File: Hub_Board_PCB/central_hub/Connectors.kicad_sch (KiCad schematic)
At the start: 16 parts, among them J1 CX90B-16P, J10 Conn_02x03_Counter_Clockwise, J3 TSM-105-01-S-DV-M-TR, J4 Screw_Terminal_01x08, J5 PH2-06-UA, J6 Screw_Terminal_01x04, J7 Screw_Terminal_01x14, SW1 RotaryEncoder_Switch

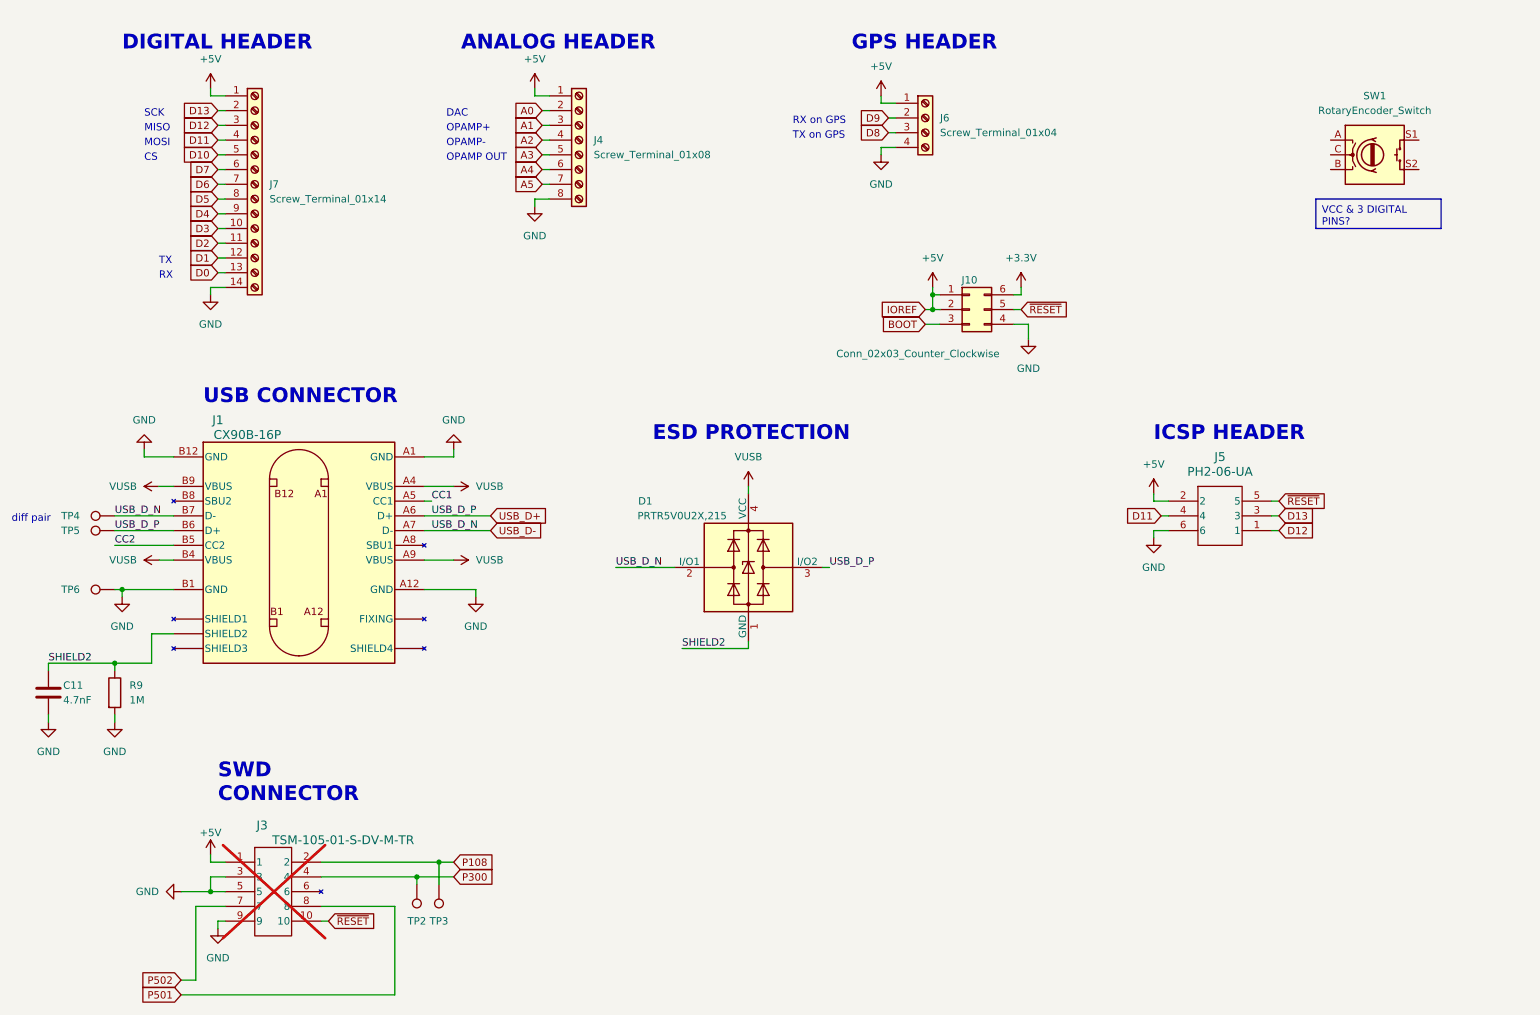
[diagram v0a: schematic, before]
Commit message: - added header for shorting VUSB and +5V
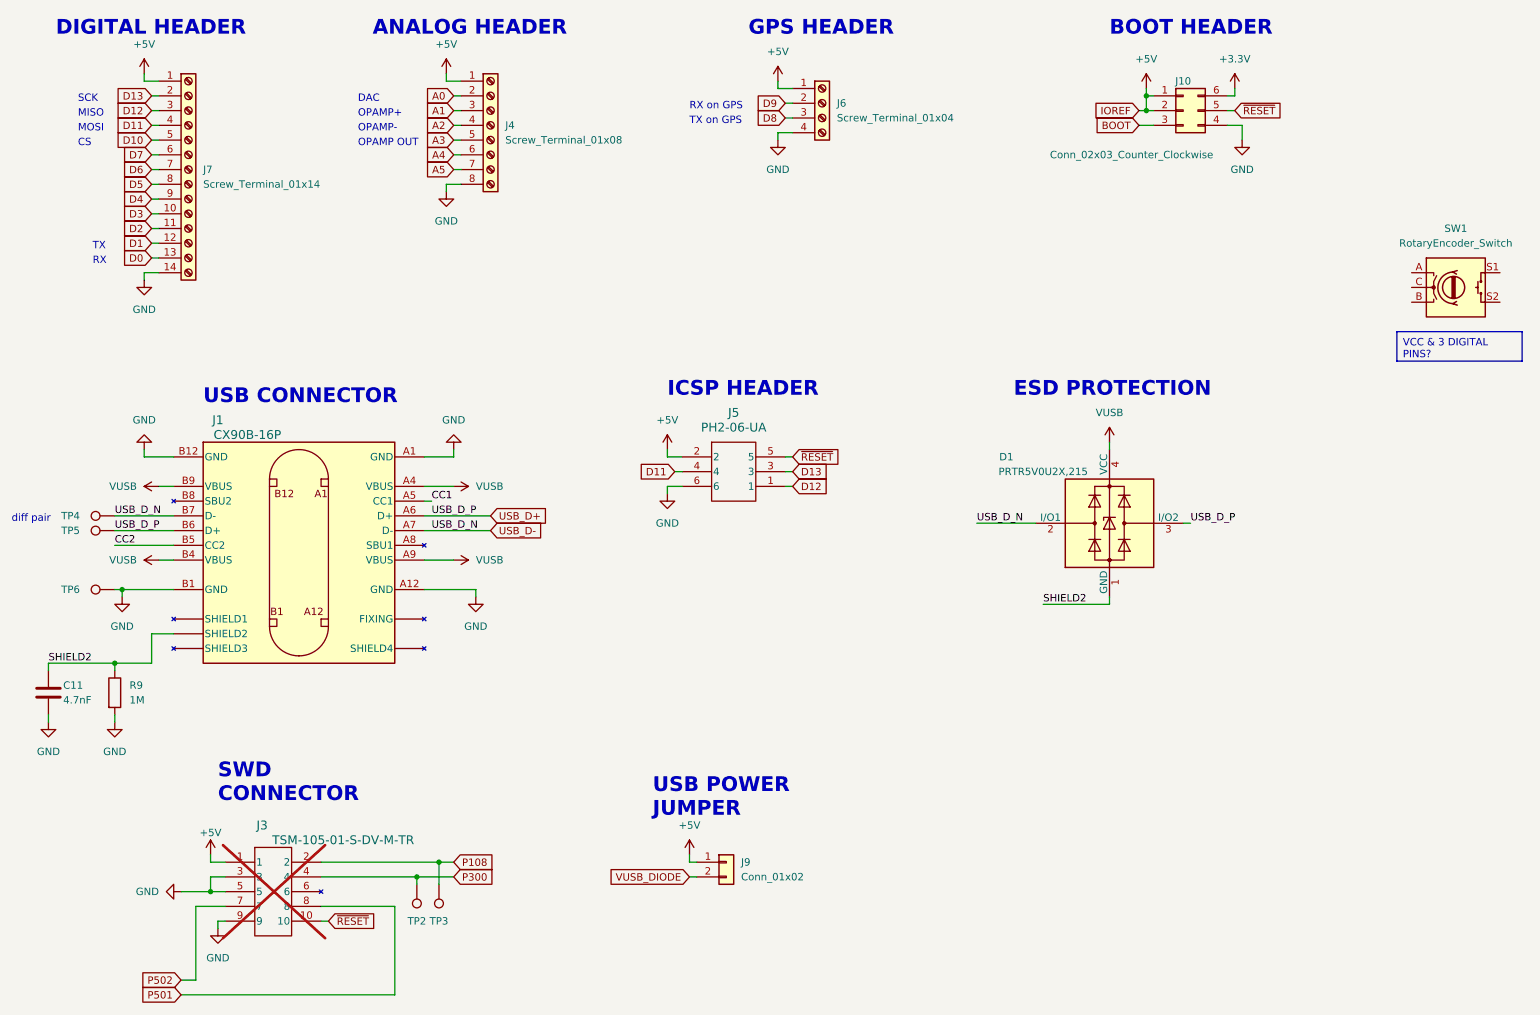
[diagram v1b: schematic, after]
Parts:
- added J9: Conn_01x02, symbol Connector_Generic:Conn_01x02
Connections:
- net +5V: now also J9.1 (Pin_1)
- new net VUSB_DIODE: J9.2 (Pin_2)
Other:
- note added: "BOOT HEADER"
- note added: "USB POWER JUMPER"
- moved on the sheet: D1, J10, J4, J5, J6, J7, SW1
